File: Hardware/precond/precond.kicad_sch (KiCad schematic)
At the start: 19 parts, among them J1 Conn_Coaxial, J2 Conn_Coaxial, U1 OPA2340, U2 MAX660

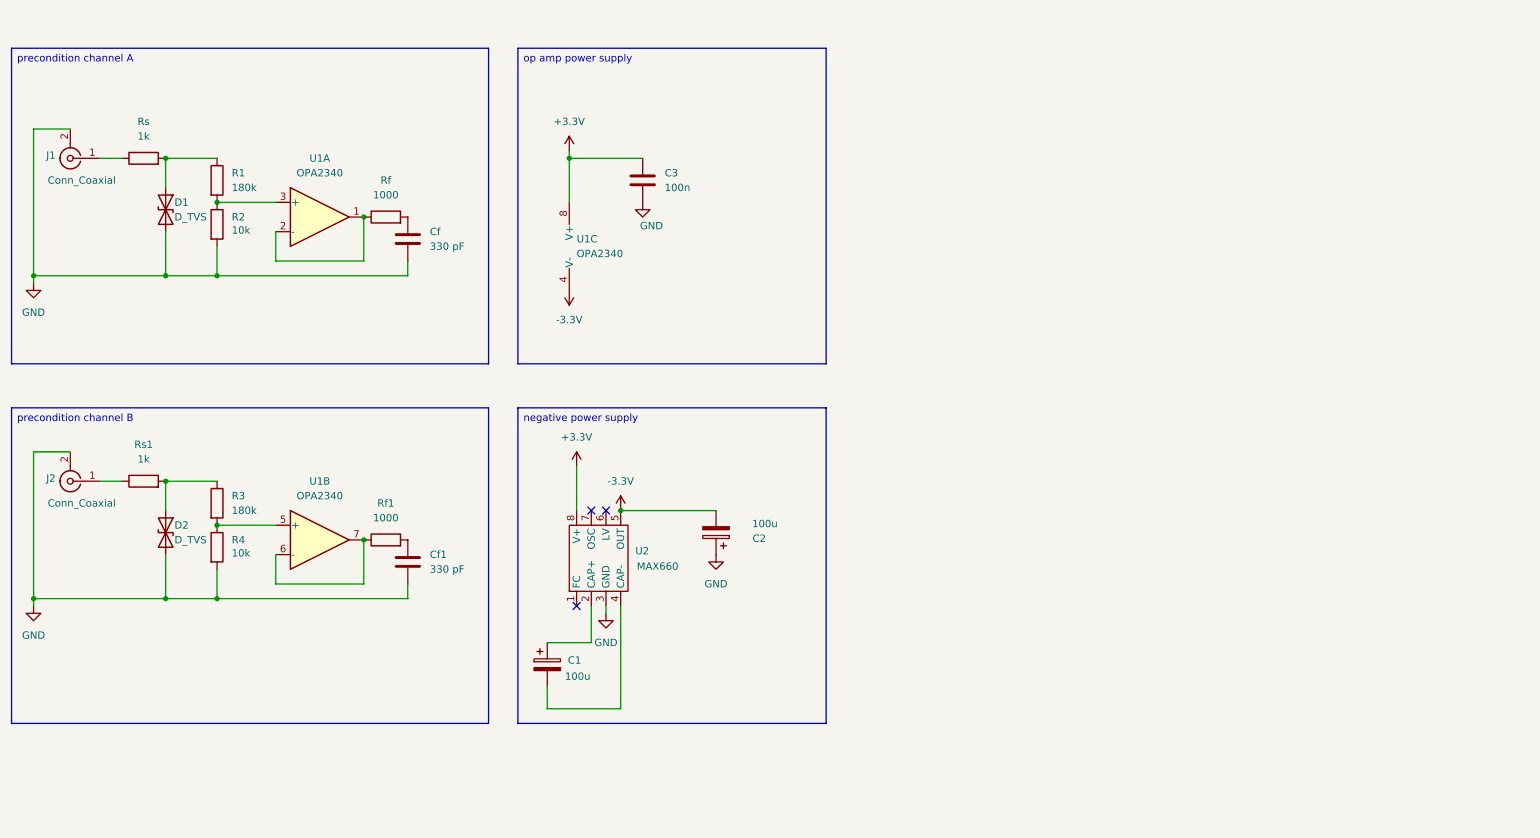
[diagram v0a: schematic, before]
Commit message: Power elec laid down, 20vpp max added
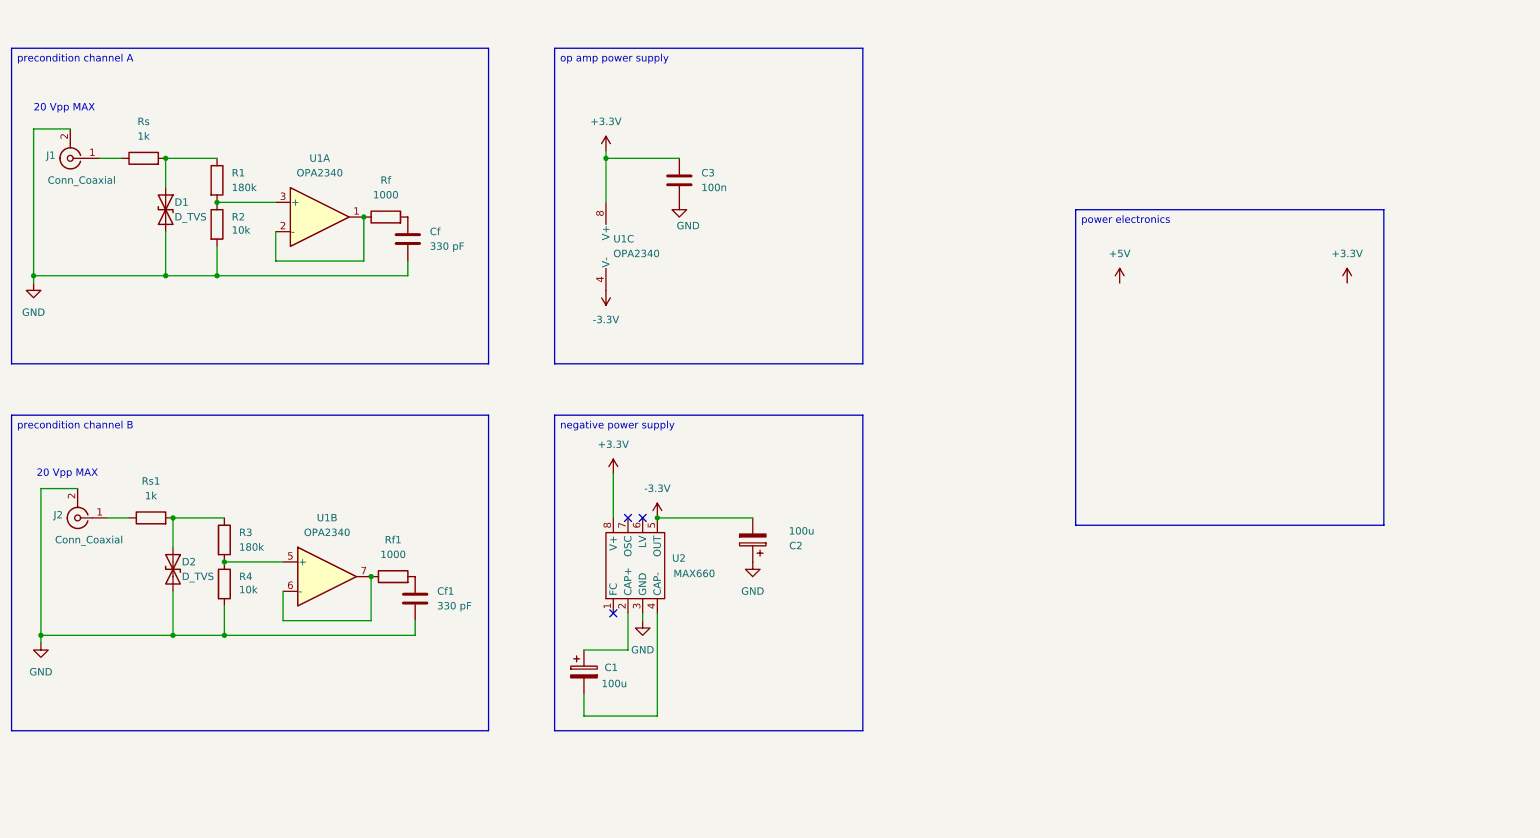
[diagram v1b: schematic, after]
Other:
- note added: "20 Vpp MAX"
- moved on the sheet: C1, C2, C3, Cf1, D2, J2, R3, R4, Rf1, Rs1, U1B, U1C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

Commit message: ahh
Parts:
- added R5, R6: 10k, symbol Device:R
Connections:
- net at D1.1 (A1), Rs.2: now also R6.1; no longer R1.1
- net at D2.1 (A1), Rs1.2: now also R5.1; no longer R3.1
- new net: R1.1, R6.2
- new net: R3.1, R5.2
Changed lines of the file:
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@@
+	)
+	(junction
+		(at 76.2 60.96)
+		(diameter 0)
+		(color 0 0 0 0)
+	)
+	(junction
+		(at 77.47 123.19)
+		(diameter 0)
+		(color 0 0 0 0)
+	)
+	(junction
+		(at 50.8 58.42)
+		(diameter 0)
+		(color 0 0 0 0)
+	)
+	(junction
+		(at 127 113.03)
+		(diameter 0)
+		(color 0 0 0 0)
+	)
+	(junction
+		(at 50.8 71.12)
+		(diameter 0)
+		(color 0 0 0 0)
+	)
+	(junction
+		(at 41.91 71.12)
+		(diameter 0)
+		(color 0 0 0 0)
 	)
 	(junction
@@
 	)
 	(junction
-		(at 76.2 60.96)
-		(diameter 0)
-		(color 0 0 0 0)
-	)
-	(junction
-		(at 77.47 123.19)
-		(diameter 0)
-		(color 0 0 0 0)
-	)
-	(junction
-		(at 50.8 58.42)
-		(diameter 0)
-		(color 0 0 0 0)
-	)
-	(junction
-		(at 127 113.03)
-		(diameter 0)
-		(color 0 0 0 0)
-	)
-	(junction
-		(at 50.8 71.12)
-		(diameter 0)
-		(color 0 0 0 0)
-	)
-	(junction
-		(at 41.91 71.12)
-		(diameter 0)
-		(color 0 0 0 0)
-	)
-	(junction
 		(at 52.07 133.35)
 		(diameter 0)
@@
 	(wire
 		(pts
-			(xy 41.91 50.8) (xy 50.8 50.8)
+			(xy 50.8 113.03) (xy 52.07 113.03)
 		)
 		(stroke
@@
 	(wire
 		(pts
-			(xy 43.18 113.03) (xy 52.07 113.03)
+			(xy 49.53 50.8) (xy 50.8 50.8)
 		)
 		(stroke
@@
 	)
 	(symbol
+		(lib_id "Device:R")
+		(at 45.72 50.8 90)
+		(unit 1)
+		(exclude_from_sim no)
+		(in_bom yes)
+		(on_board yes)
+		(dnp no)
+		(property "Reference" "R6"
+			(at 44.4499 48.26 0)
+			(effects
+				(font
+					(size 1.27 1.27)
+				)
+				(justify left)
+			)
+		)
+		(property "Value" "10k"
+			(at 46.736 48.26 0)
+			(effects
+				(font
+					(size 1.27 1.27)
+				)
+				(justify left)
+			)
+		)
+		(property "Footprint" ""
+			(at 45.72 52.578 90)
+			(effects
+				(font
+					(size 1.27 1.27)
+				)
+				(hide yes)
+			)
+		)
+		(property "Datasheet" "~"
+			(at 45.72 50.8 0)
+			(effects
+				(font
+					(size 1.27 1.27)
+				)
+				(hide yes)
+			)
+		)
+		(property "Description" "Resistor"
+			(at 45.72 50.8 0)
+			(effects
+				(font
+					(size 1.27 1.27)
+				)
+				(hide yes)
+			)
+		)
+		(pin "1"
+		)
+		(pin "2"
+		)
+		(instances
+			(project "precond"
+				(path "/1b3d796b-04c2-4e3e-92b7-8b7b30957c7c"
+					(reference "R6")
+					(unit 1)
+				)
+			)
+		)
+	)
+	(symbol
 		(lib_id "Device:C_Polarized")
 		(at 114.3 139.7 0)
@@
 					(unit 1)
 				)
+			)
+		)
+	)
+	(symbol
+		(lib_id "Device:R")
+		(at 46.99 113.03 90)
+		(unit 1)
+		(exclude_from_sim no)
+		(in_bom yes)
+		(on_board yes)
+		(dnp no)
+		(property "Reference" "R5"
+			(at 45.7199 110.49 0)
+			(effects
+				(font
+					(size 1.27 1.27)
+				)
+				(justify left)
+			)
+		)
+		(property "Value" "10k"
+			(at 48.006 110.49 0)
+			(effects
+				(font
+					(size 1.27 1.27)
+				)
+				(justify left)
+			)
+		)
+		(property "Footprint" ""
+			(at 46.99 114.808 90)
+			(effects
+				(font
+					(size 1.27 1.27)
+				)
+				(hide yes)
+			)
+		)
+		(property "Datasheet" "~"
+			(at 46.99 113.03 0)
+			(effects
+				(font
+					(size 1.27 1.27)
+				)
+				(hide yes)
+			)
+		)
+		(property "Description" "Resistor"
+			(at 46.99 113.03 0)
+			(effects
+				(font
+					(size 1.27 1.27)
+				)
+				(hide yes)
+			)
+		)
+		(pin "1"
+		)
+		(pin "2"
+		)
+		(instances
+			(project "precond"
+				(path "/1b3d796b-04c2-4e3e-92b7-8b7b30957c7c"
+					(reference "R5")
+					(unit 1)
+				)

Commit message: buck
buck
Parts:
- added C4: 680uF, symbol Device:C
- added C5: 220uF, symbol Device:C
- added D3: 1N5822, Diode_THT:D_DO-201AD_P15.24mm_Horizontal, symbol Diode:1N5822
- added L1: 33uH, symbol Device:L
- added U3: LM2596S-3.3, Package_TO_SOT_SMD:TO-263-5_TabPin3, symbol Regulator_Switching:LM2596S-3.3
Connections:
- net +3.3V: now also C5.1, L1.2, U3.4 (FB)
- net +5V: now also C4.1, U3.1 (VIN)
- net GND: now also C4.2, C5.2, D3.2 (A), U3.3 (GND), U3.5 (~{ON}/OFF)
- new net: D3.1 (K), L1.1, U3.2 (OUT)
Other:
- note added: "Buck converter"

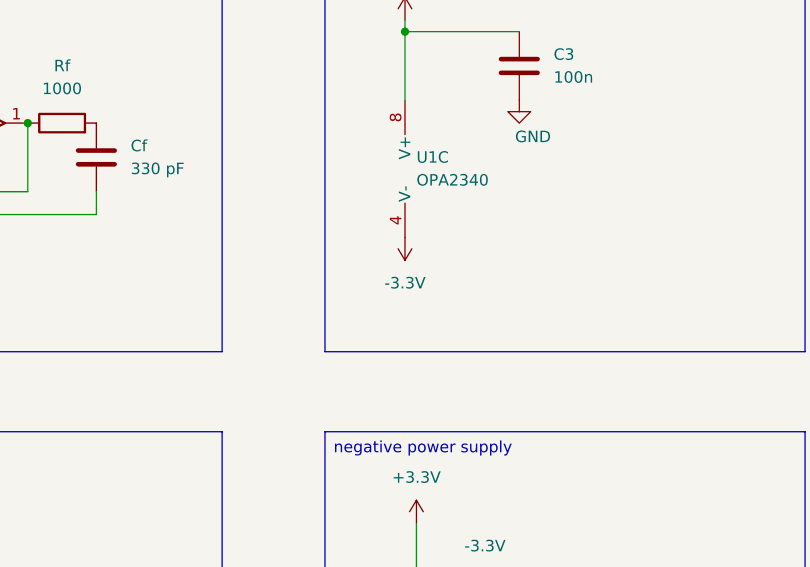
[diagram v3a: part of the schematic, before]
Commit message: precond simulation finished
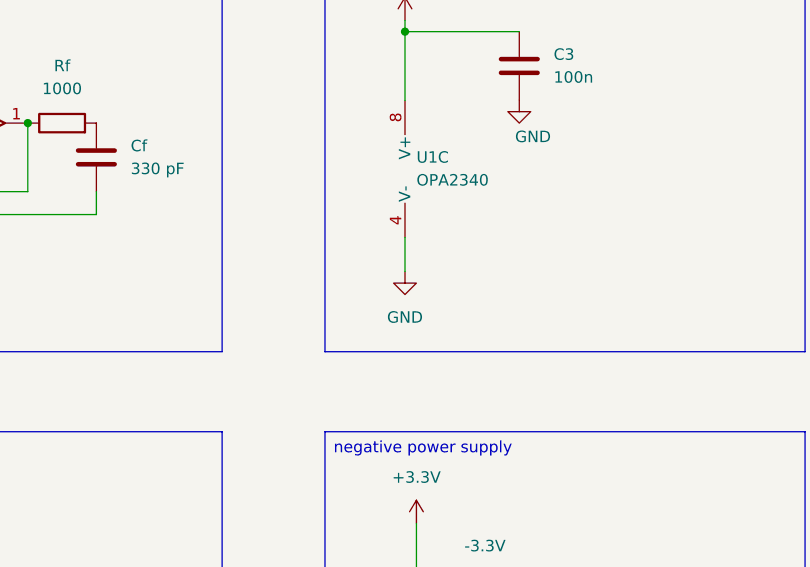
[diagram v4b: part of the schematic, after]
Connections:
- net -3.3V: no longer U1.4 (V-)
- net GND: now also U1.4 (V-)
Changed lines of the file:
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@@
+	(wire
+		(pts
+			(xy 118.11 73.66) (xy 118.11 77.47)
+		)
+		(stroke
+			(width 0)
+			(type default)
+		)
+	)
 	(wire
 		(pts
@@
 	)
 	(symbol
+		(lib_id "power:GND")
+		(at 118.11 77.47 0)
+		(unit 1)
+		(exclude_from_sim no)
+		(in_bom yes)
+		(on_board yes)
+		(dnp no)
+		(fields_autoplaced yes)
+		(property "Reference" "#PWR06"
+			(at 118.11 83.82 0)
+			(effects
+				(font
+					(size 1.27 1.27)
+				)
+				(hide yes)
+			)
+		)
+		(property "Value" "GND"
+			(at 118.11 82.55 0)
+			(effects
+				(font
+					(size 1.27 1.27)
+				)
+			)
+		)
+		(property "Footprint" ""
+			(at 118.11 77.47 0)
+			(effects
+				(font
+					(size 1.27 1.27)
+				)
+				(hide yes)
+			)
+		)
+		(property "Datasheet" ""
+			(at 118.11 77.47 0)
+			(effects
+				(font
+					(size 1.27 1.27)
+				)
+				(hide yes)
+			)
+		)
+		(property "Description" "Power symbol creates a global label with name \"GND\" , ground"
+			(at 118.11 77.47 0)
+			(effects
+				(font
+					(size 1.27 1.27)
+				)
+				(hide yes)
+			)
+		)
+		(pin "1"
+		)
+		(instances
+			(project "precond"
+				(path "/1b3d796b-04c2-4e3e-92b7-8b7b30957c7c"
+					(reference "#PWR06")
+					(unit 1)
+				)
+			)
+		)
+	)
+	(symbol
 		(lib_id "power:+3.3V")
 		(at 119.38 105.41 0)
@@
 					(unit 1)
 				)
-			)
-		)
-	)
-	(symbol
-		(lib_id "power:+3.3V")
-		(at 118.11 73.66 180)
-		(unit 1)
-		(exclude_from_sim no)
-		(in_bom yes)
-		(on_board yes)
-		(dnp no)
-		(fields_autoplaced yes)
-		(property "Reference" "#PWR06"
-			(at 118.11 69.85 0)
-			(effects
-				(font
-					(size 1.27 1.27)
-				)
-				(hide yes)
-			)
-		)
-		(property "Value" "-3.3V"
-			(at 118.11 78.74 0)
-			(effects
-				(font
-					(size 1.27 1.27)
-				)
-			)
-		)
-		(property "Footprint" ""
-			(at 118.11 73.66 0)
-			(effects
-				(font
-					(size 1.27 1.27)
-				)
-				(hide yes)
-			)
-		)
-		(property "Datasheet" ""
-			(at 118.11 73.66 0)
-			(effects
-				(font
-					(size 1.27 1.27)
-				)
-				(hide yes)
-			)
-		)
-		(property "Description" "Power symbol creates a global label with name \"+3.3V\""
-			(at 118.11 73.66 0)
-			(effects
-				(font
-					(size 1.27 1.27)
-				)
-				(hide yes)
-			)
-		)
-		(pin "1"
-		)
-		(instances
-			(project "precond"
-				(path "/1b3d796b-04c2-4e3e-92b7-8b7b30957c7c"
-					(reference "#PWR06")
-					(unit 1)
-				)

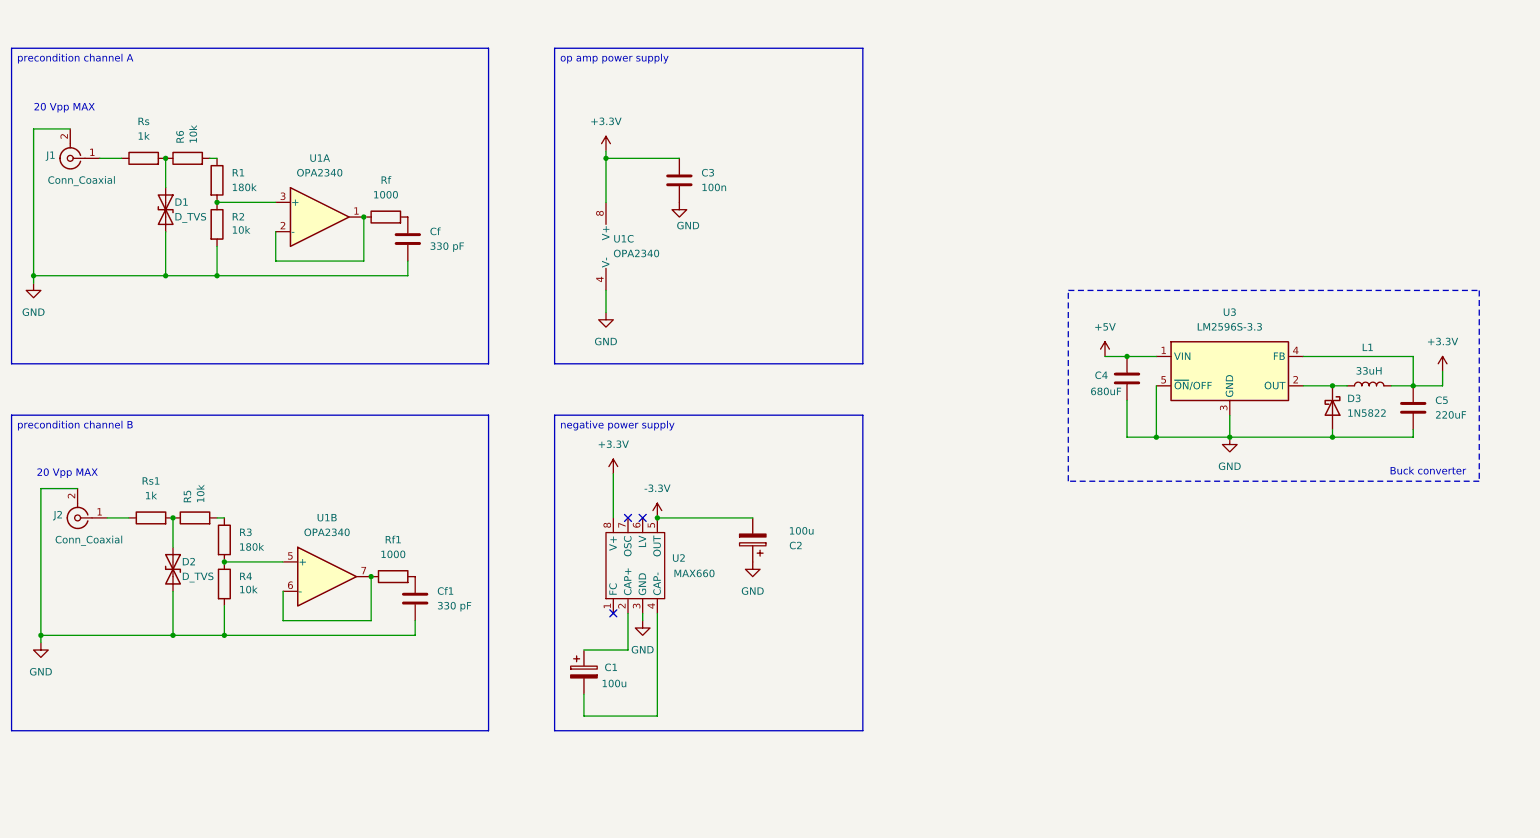
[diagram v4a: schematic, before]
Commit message: changes to op-amp PCB. needs footprints!
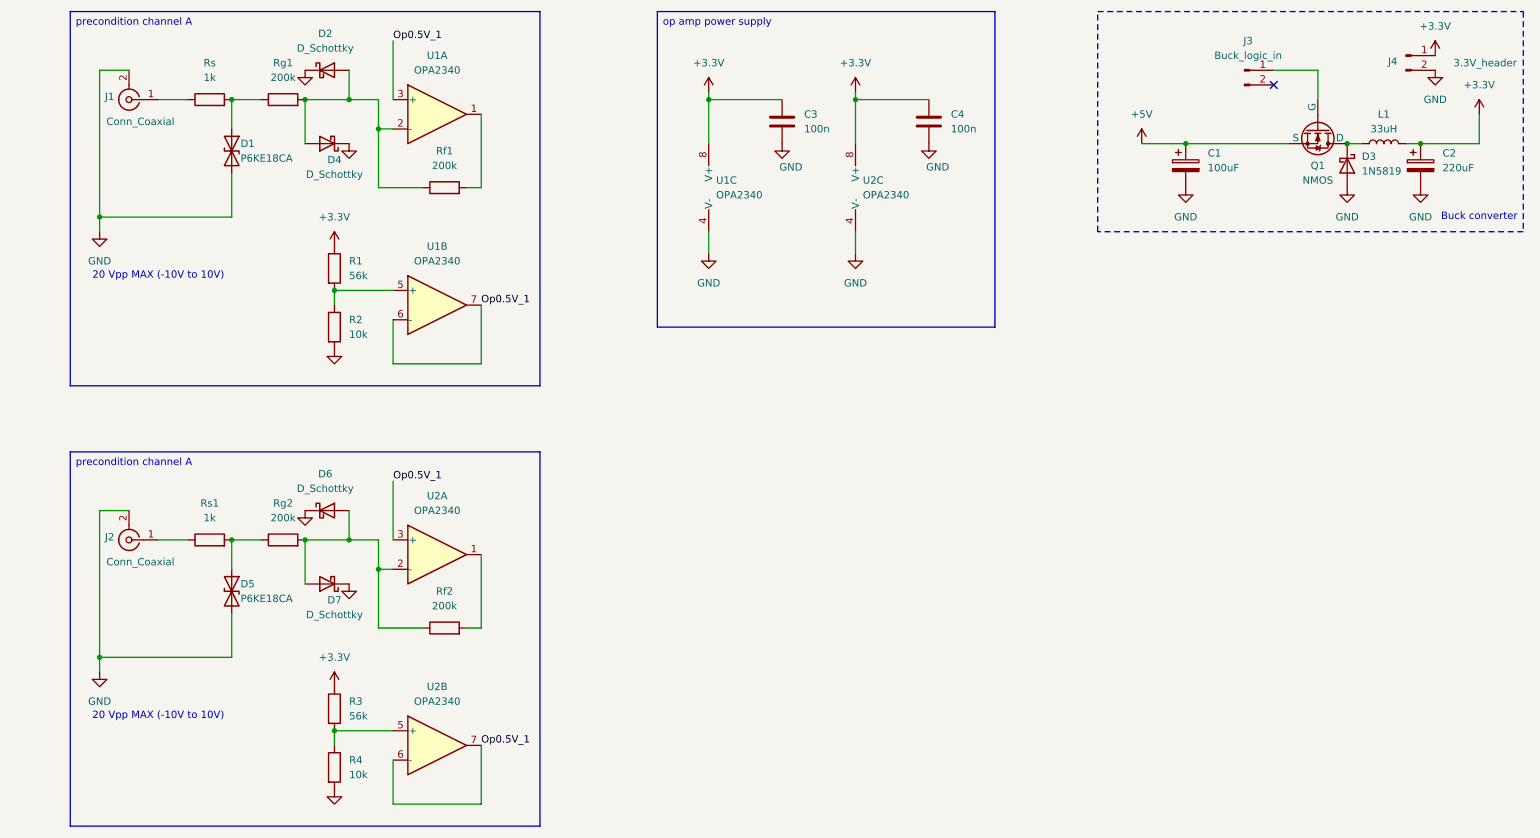
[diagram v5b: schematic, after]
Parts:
- removed C5: 220uF, symbol Device:C
- removed Cf, Cf1: 330 pF, symbol Device:C
- removed D2: D_TVS, symbol Device:D_TVS
- removed D3: 1N5822, Diode_THT:D_DO-201AD_P15.24mm_Horizontal, symbol Diode:1N5822
- removed R5, R6: 10k, symbol Device:R
- removed Rf: 1000, symbol Device:R
- removed U2: MAX660, Package_SO:SOIC-8-1EP_3.9x4.9mm_P1.27mm_EP2.29x3mm, symbol max660:MAX660CPA+
- removed U3: LM2596S-3.3, Package_TO_SOT_SMD:TO-263-5_TabPin3, symbol Regulator_Switching:LM2596S-3.3
- added D2, D4, D6, D7: D_Schottky, symbol Device:D_Schottky
- added D3: 1N5819, Diode_THT:D_DO-41_SOD81_P10.16mm_Horizontal, symbol Diode:1N5819
- added D5: P6KE18CA, symbol Device:D_TVS
- added J3: Buck_logic_in, symbol Connector:Conn_01x02_Pin
- added J4: 3.3V_header, symbol Connector:Conn_01x02_Pin
- added Q1: NMOS, symbol Simulation_SPICE:NMOS
- added Rf2, Rg1, Rg2: 200k, symbol Device:R
- added U2: OPA2340, symbol Amplifier_Operational:OPA2340
- C1: value 100u -> 100uF
- C2: value 100u -> 220uF
- C4: value 680uF -> 100n
- D1: value D_TVS -> P6KE18CA
- R1, R3: value 180k -> 56k
- Rf1: value 1000 -> 200k
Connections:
- net -3.3V is gone; now on net GND: C2.2
- net +3.3V: now also C2.1, C4.1, R1.1, R3.1, J4.1 (Pin_1), U2.8 (V+)
- net +5V: now also C1.1, Q1.3 (S); no longer C4.1
- net GND: now also C1.2, D2.1 (K), D3.2 (A), D4.1 (K), D5.2 (A2), D6.1 (K), D7.1 (K), J4.2 (Pin_2), U2.4 (V-); no longer C2.1
- net at R1.2, R2.1: now also U1.5 (+); no longer U1.3 (+)
- net at U1.2 (-): now also Rf1.1, D2.2 (A), D4.2 (A), Rg1.2; no longer U1.1
- net at D1.1 (A1), Rs.2: now also Rg1.1
- net at R3.2, R4.1: now also U2.5 (+); no longer U1.5 (+)
- net Op0.5V_1: now reaches U1.6 (-), U1.7
- net Op0.5V_1: now also U1.3 (+), U2.3 (+), U2.6 (-), U2.7; no longer Rf1.1
- net at Rf1.2: now also U1.1
- net at L1.1: now also D3.1 (K), Q1.1 (D)
- net at Rs1.2: now also D5.1 (A1), Rg2.1
- new net: Rf2.2, U2.1
- new net: D6.2 (A), D7.2 (A), Rf2.1, Rg2.2, U2.2 (-)
- new net: J3.1 (Pin_1), Q1.2 (G)
- no-connect marks 3 -> 1
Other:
- note added: "20 Vpp MAX (-10V to 10V)"
- note removed: "20 Vpp MAX"
- moved on the sheet: C3, D1, J1, Rs, U1C
